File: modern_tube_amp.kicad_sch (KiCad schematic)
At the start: 88 parts, among them J1 XLR, J2 RCA, J3 Conn_01x02_Socket, J4 Conn_01x02_Socket, J5 connector to power board (mol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, J6 Conn_01x02_Socket, SW1 SW_Push, SW2 SW_SPST, T1 Transformer_Audio, T2 Transformer_Audio, T3 Transformer_Audio, T4 1650RA, T5 Transformer_Audio, T6 Transformer_Audio, U1 74HC14, U3 12ax7, U4 CD4066BM96, U5 kt88, U6 kt88, U7 LM317_BIAS

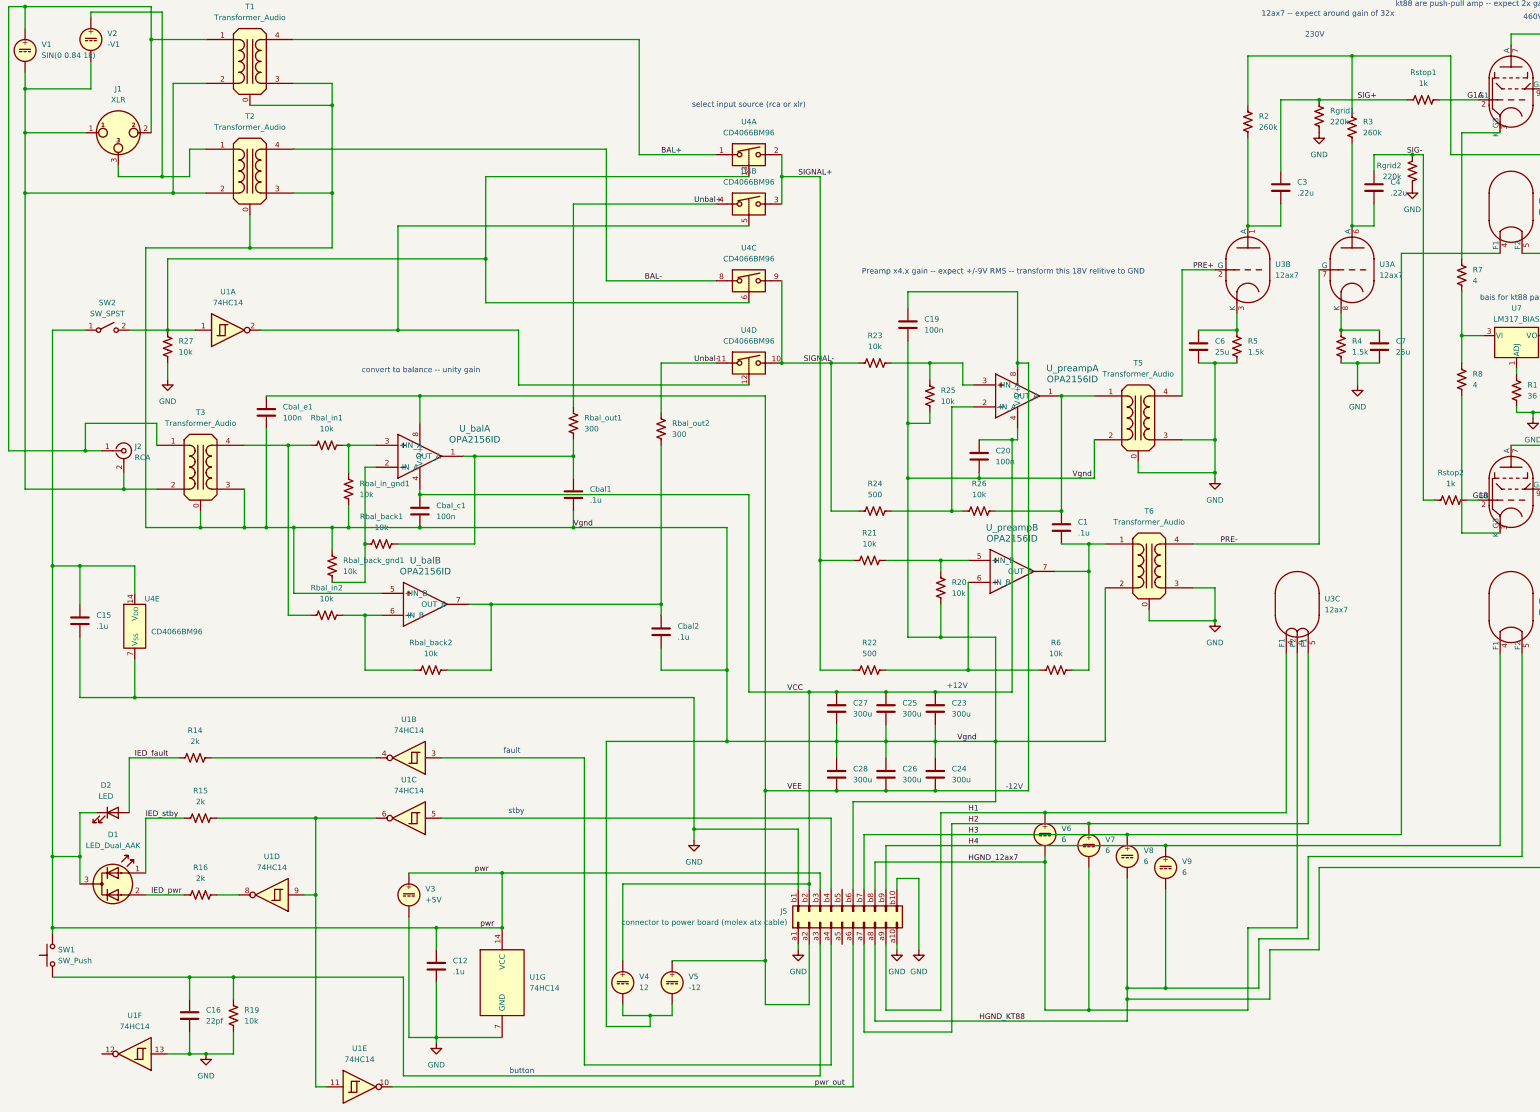
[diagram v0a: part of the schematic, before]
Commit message: update sch to split GND
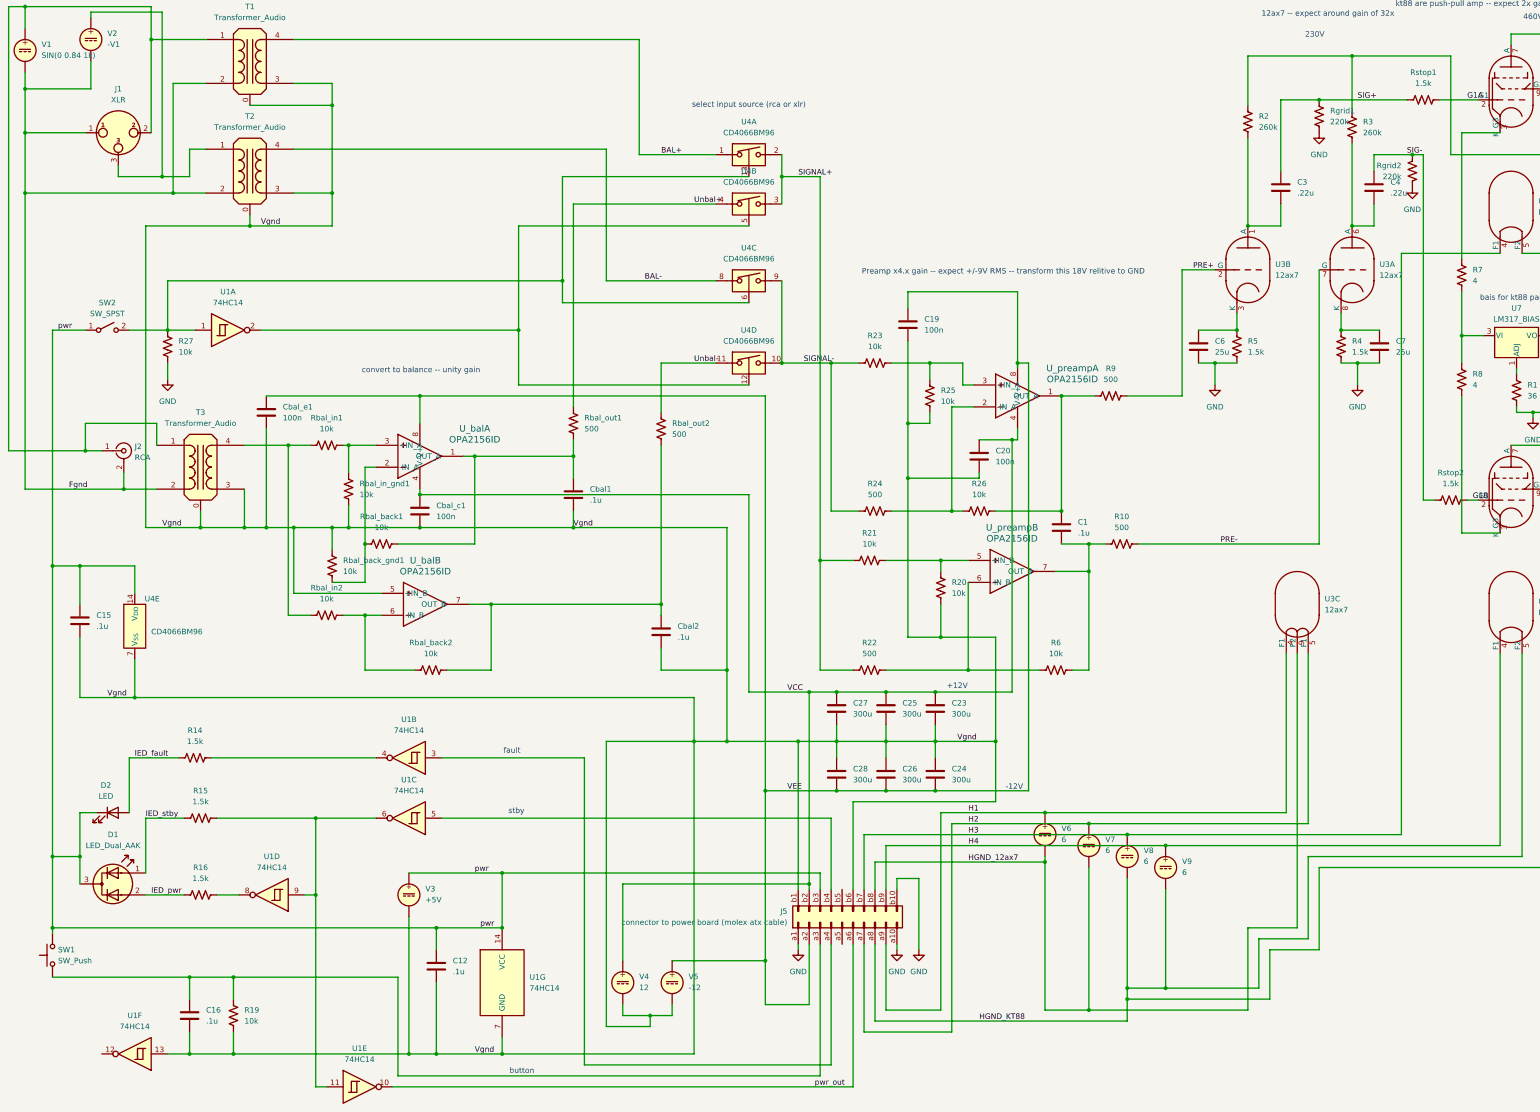
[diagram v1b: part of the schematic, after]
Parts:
- removed T5, T6: Transformer_Audio, symbol Device:Transformer_Audio
- added R10, R9: 500, symbol Device:R_US
- C16: value 22pf -> .1u
- R14, R15, R16: value 2k -> 1.5k
- Rbal_out1, Rbal_out2: value 300 -> 500
- Rstop1, Rstop2: value 1k -> 1.5k
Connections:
- net GND: no longer C12.2, C15.2, C16.2, J5.b1 (Pin_b1), R19.2, U1.13, U1.7 (GND), U4.7 (V_{SS}), V3.2
- net PRE+: now also R9.2
- net PRE-: now also R10.2
- net Vgnd: now also C12.2, C15.2, C16.2, J5.b1 (Pin_b1), R19.2, U1.13, U1.7 (GND), U4.7 (V_{SS}), V3.2
- net at C1.2, R6.2, U_preamp.7 (OUT_B): now also R10.1
- net Fgnd: now reaches J1.1, J2.2 (Ext), T1.2 (AB), T2.2 (AB), T3.2 (AB), V1.2, V2.2
- net at C1.1, R26.2, U_preamp.1 (OUT_A): now also R9.1

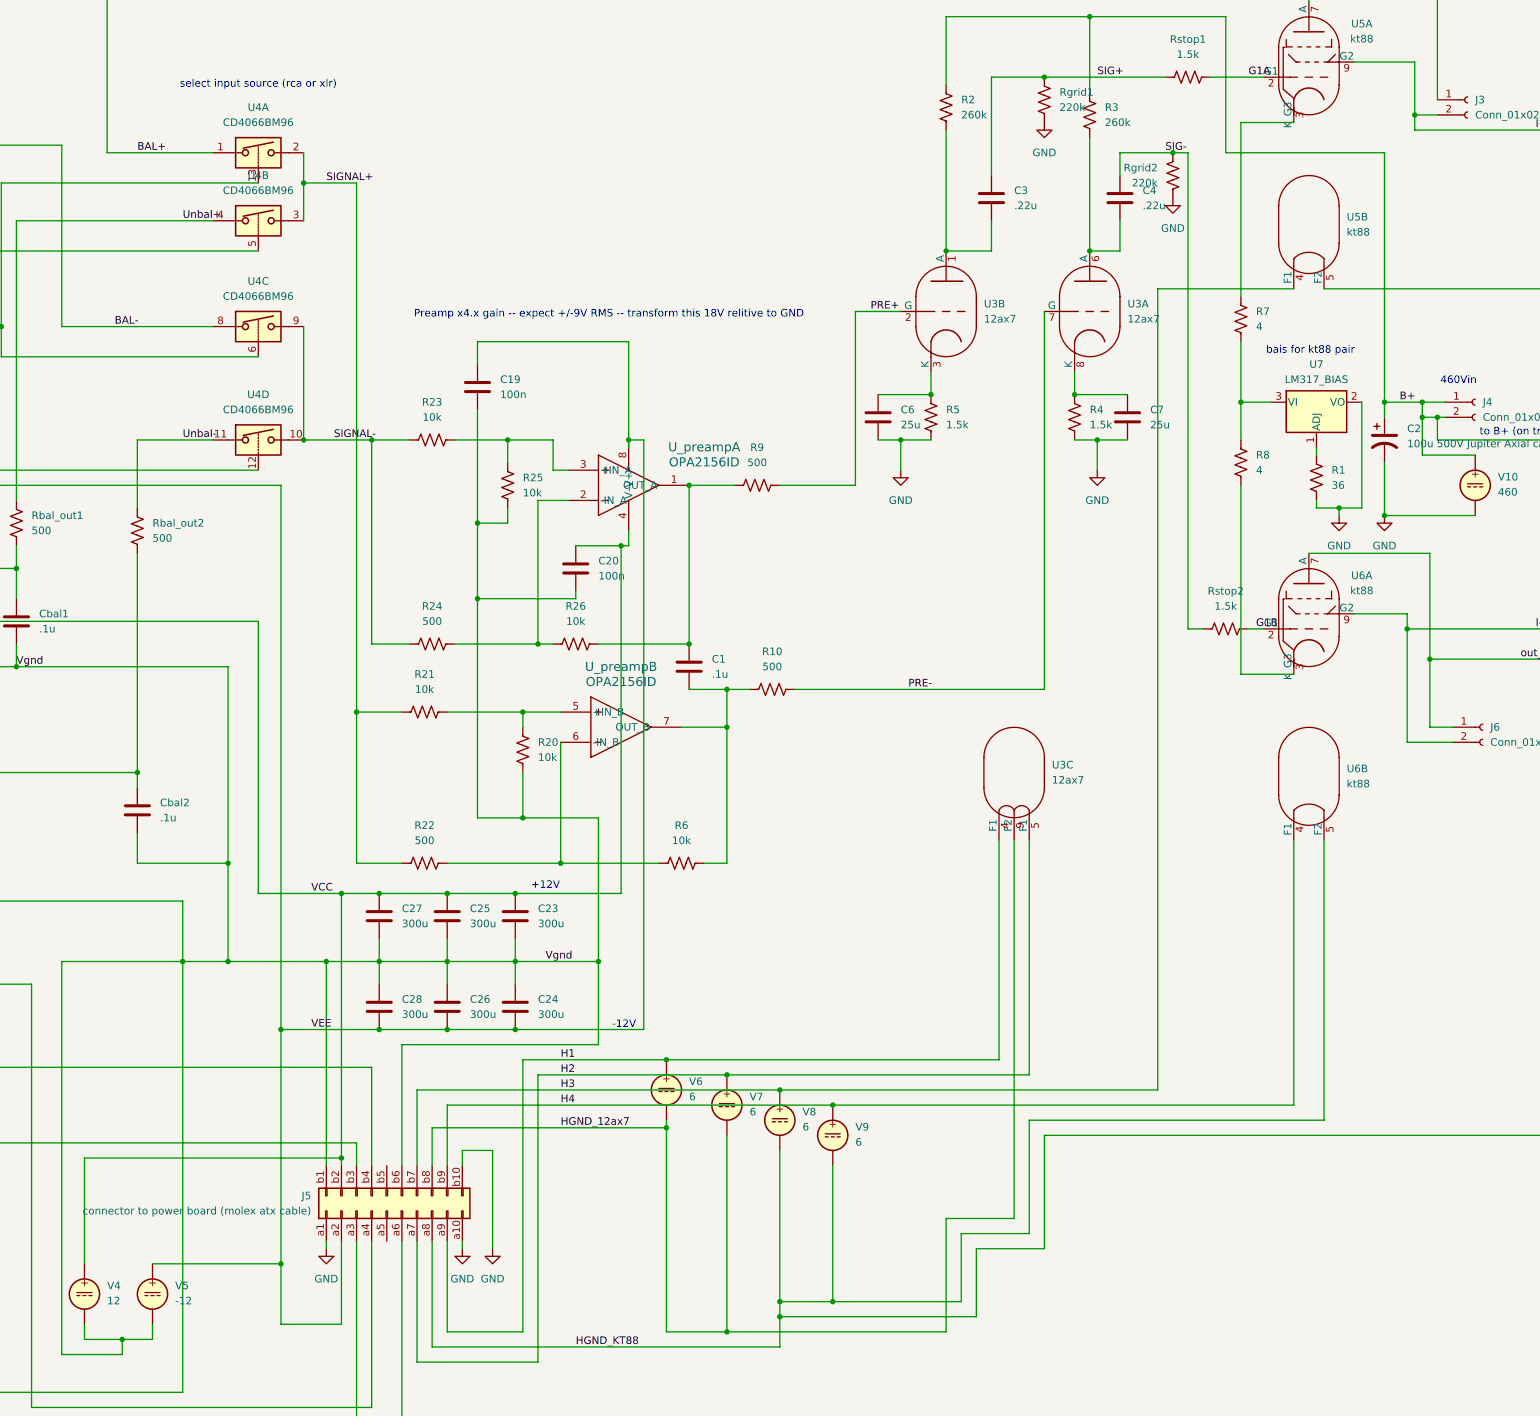
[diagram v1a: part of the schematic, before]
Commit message: get 12ax7up -- don't like voltage, do like shape
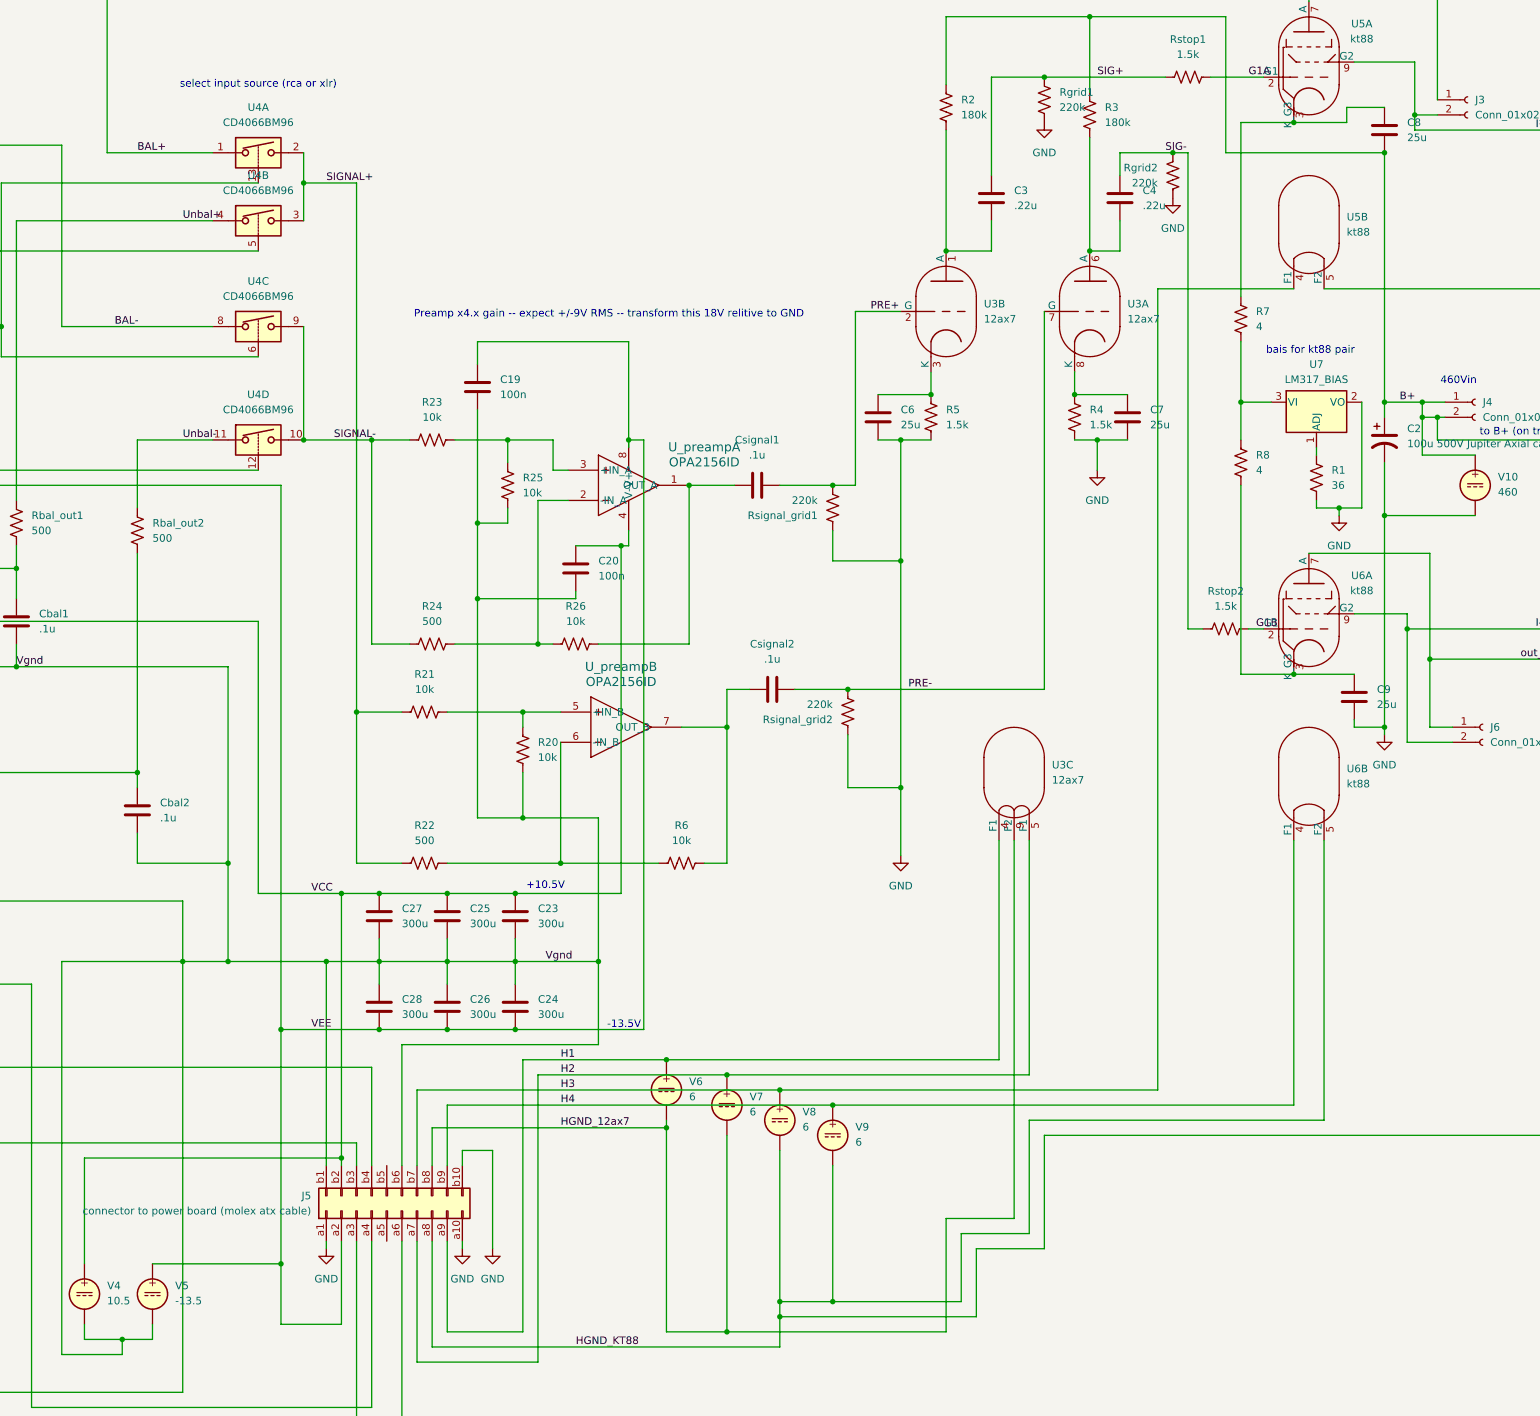
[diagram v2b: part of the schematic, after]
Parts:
- removed C1: .1u, symbol Device:C
- removed R10, R9: 500, symbol Device:R_US
- added C8, C9: 25u, symbol Device:C
- added Csignal1, Csignal2: .1u, symbol Device:C
- added Rsignal_grid1, Rsignal_grid2: 220k, symbol Device:R_US
- R2, R3: value 260k -> 180k
- V4: value 12 -> 10.5
- V5: value -12 -> -13.5
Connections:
- net B+: now also C8.2
- net GND: now also C9.2, Rsignal_grid1.1, Rsignal_grid2.1
- net PRE+: now also Csignal1.2, Rsignal_grid1.2
- net PRE-: now also Csignal2.2, Rsignal_grid2.2
- net at R7.1, U5.3 (K_G3): now also C8.1
- net at R6.2, U_preamp.7 (OUT_B): now also Csignal2.1
- net at R8.2, U6.3 (K_G3): now also C9.1
- net at R26.2, U_preamp.1 (OUT_A): now also Csignal1.1
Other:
- note added: "+10.5V"
- note added: "-13.5V"
- note removed: "+12V"
- note removed: "-12V"
